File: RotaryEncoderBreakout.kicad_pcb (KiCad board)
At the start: 2 copper layers, 33 x 34.3 mm, 17 parts, among them J1 Conn_01x04_Male, J2 Conn_01x04_Male, J3 Conn_01x05_Male, SW1 RotaryEncoder_Switch_RGB, U1 WS2811

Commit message: Silkscreen refinement
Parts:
- SW1: value RotaryEncoder_Switch_RGB -> EC12PLRGB
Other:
- board text added: "J3: 1=PC3 2=Din 3=Dout Short 1-2 for Din=PC3 Short 4-5 for 400KHz / Open for 800KHz"
- board text removed: "J3: Din=2 Dout=3 Short 1-2 for Din=PC3 Short 4-5 for 400KHz / Open for 800KHz"
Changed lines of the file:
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@@
     (links 0)
     (no_connects 0)
-    (area 106.921 51.041 145.274 87.705001)
+    (area 109.779999 53.264999 142.950001 87.705001)
     (thickness 1.6)
     (drawings 17)
@@
       (effects (font (size 1 1) (thickness 0.15)))
     )
-    (fp_text value RotaryEncoder_Switch_RGB (at 12.065 1.27 90) (layer F.Fab)
-      (effects (font (size 1 1) (thickness 0.15)))
+    (fp_text value EC12PLRGB (at 6.858 -4.445 90) (layer F.SilkS)
+      (effects (font (size 0.635 0.635) (thickness 0.15)))
     )
     (fp_line (start -6.223 6.604) (end 6.223 6.604) (layer F.CrtYd) (width 0.15))
@@
     (descr "Through hole straight pin header, 1x05, 2.54mm pitch, single row")
     (tags "Through hole pin header THT 1x05 2.54mm single row")
-    (fp_text reference J3 (at 0 -3.175 360) (layer F.SilkS)
+    (fp_text reference J3 (at 0 -3.175 450) (layer F.SilkS)
       (effects (font (size 1 1) (thickness 0.15)))
     )
@@
       (effects (font (size 1 1) (thickness 0.15)))
     )
-    (fp_text value 10K (at 1.905 1.905) (layer F.SilkS)
+    (fp_text value 10K (at 1.27 1.905) (layer F.SilkS)
       (effects (font (size 0.635 0.635) (thickness 0.15)))
     )
@@
       (effects (font (size 1 1) (thickness 0.15)))
     )
-    (fp_text value 33 (at 1.905 1.905) (layer F.SilkS)
+    (fp_text value 33 (at 1.27 1.905) (layer F.SilkS)
       (effects (font (size 0.635 0.635) (thickness 0.15)))
     )
@@
       (effects (font (size 1 1) (thickness 0.15)))
     )
-    (fp_text value WS2811 (at 0 3.5 90) (layer F.Fab)
-      (effects (font (size 1 1) (thickness 0.15)))
+    (fp_text value WS2811 (at 0 -3.175 90) (layer F.SilkS)
+      (effects (font (size 0.635 0.635) (thickness 0.15)))
     )
     (fp_line (start -0.95 -2.45) (end 1.95 -2.45) (layer F.Fab) (width 0.15))
@@
     (effects (font (size 1.27 1.27) (thickness 0.3)) (justify mirror))
   )
-  (gr_text "J3: Din=2 Dout=3 Short 1-2 for Din=PC3\nShort 4-5 for 400KHz / Open for 800KHz" (at 140.97 70.485 90) (layer F.SilkS)
-    (effects (font (size 0.762 0.762) (thickness 0.1905)))
+  (gr_text "J3: 1=PC3 2=Din 3=Dout Short 1-2 for Din=PC3\nShort 4-5 for 400KHz / Open for 800KHz" (at 140.97 71.755 90) (layer F.SilkS)
+    (effects (font (size 0.635 0.635) (thickness 0.15875)))
   )
   (gr_arc (start 114.935 78.867) (end 114.935 77.597) (angle 90) (layer Edge.Cuts) (width 0.15))
   (gr_line (start 116.205 78.867) (end 116.205 87.63) (layer Edge.Cuts) (width 0.15))
   (gr_line (start 109.855 77.597) (end 114.935 77.597) (layer Edge.Cuts) (width 0.15))
-  (gr_text PC0 (at 115.57 68.326) (layer F.SilkS)
+  (gr_text PC0 (at 115.824 68.072) (layer F.SilkS)
     (effects (font (size 0.635 0.635) (thickness 0.127)))
   )
-  (gr_text PC1 (at 115.57 70.866) (layer F.SilkS)
+  (gr_text PC1 (at 115.824 70.612) (layer F.SilkS)
     (effects (font (size 0.635 0.635) (thickness 0.127)))
   )
-  (gr_text PC2 (at 115.57 73.406) (layer F.SilkS)
+  (gr_text PC2 (at 115.824 73.152) (layer F.SilkS)
     (effects (font (size 0.635 0.635) (thickness 0.127)))
   )
-  (gr_text 5V (at 115.57 55.245) (layer F.SilkS)
+  (gr_text 5V (at 115.824 55.245) (layer F.SilkS)
     (effects (font (size 0.635 0.635) (thickness 0.127)))
   )
-  (gr_text GND (at 115.57 57.785) (layer F.SilkS)
+  (gr_text GND (at 115.824 57.785) (layer F.SilkS)
     (effects (font (size 0.635 0.635) (thickness 0.127)))
   )
-  (gr_text GND (at 115.57 60.325) (layer F.SilkS)
+  (gr_text GND (at 115.824 60.325) (layer F.SilkS)
     (effects (font (size 0.635 0.635) (thickness 0.127)))
   )
-  (gr_text PC3 (at 115.57 75.946) (layer F.SilkS)
+  (gr_text PC3 (at 115.824 75.692) (layer F.SilkS)
     (effects (font (size 0.635 0.635) (thickness 0.127)))
   )
-  (gr_text Vin (at 115.57 62.865) (layer F.SilkS)
+  (gr_text Vin (at 115.824 62.865) (layer F.SilkS)
     (effects (font (size 0.635 0.635) (thickness 0.127)))
   )

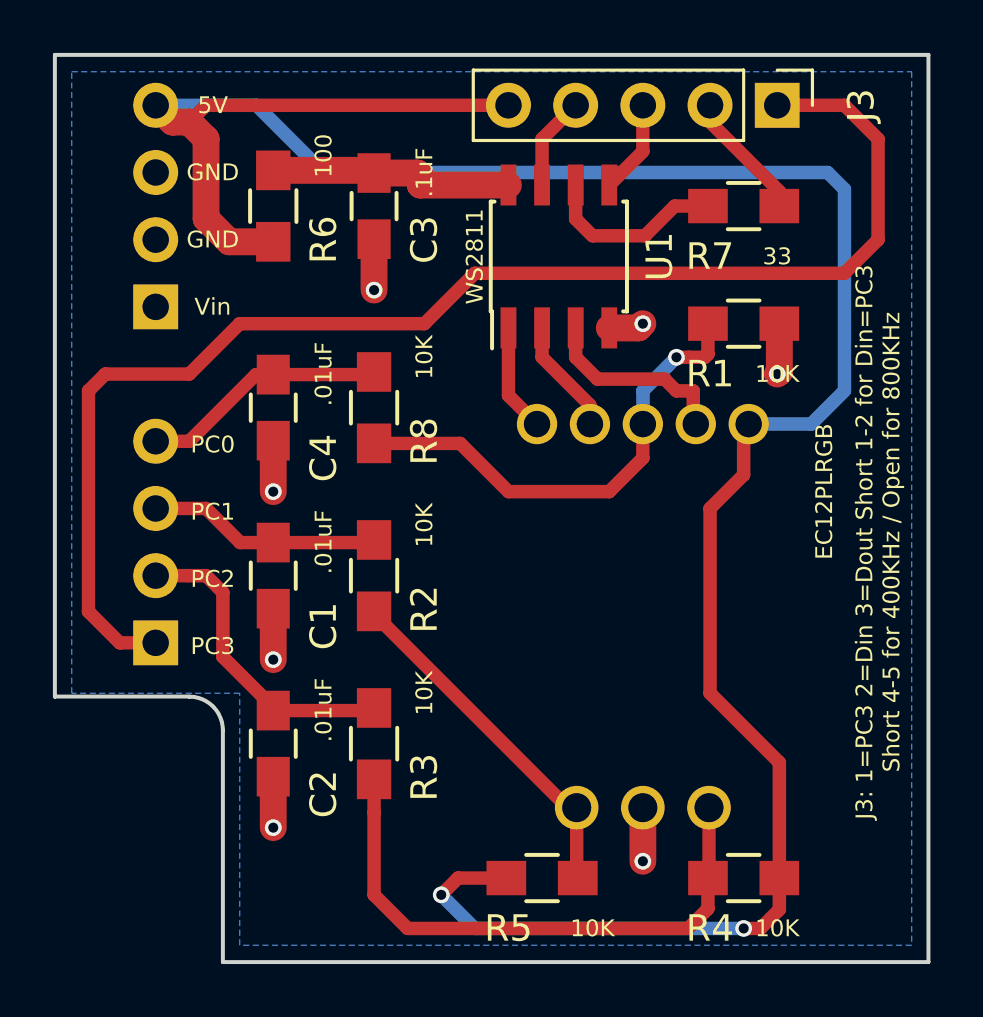
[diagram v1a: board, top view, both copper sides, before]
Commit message: Update component values
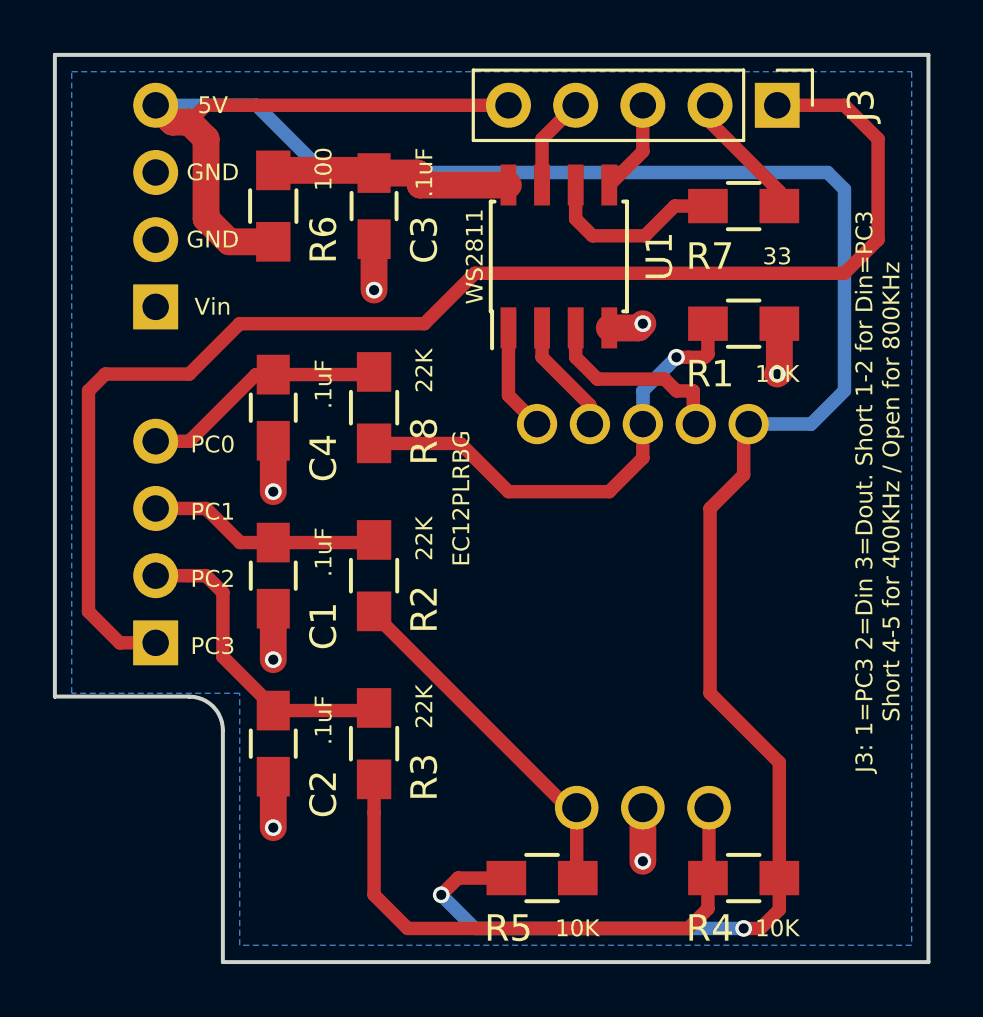
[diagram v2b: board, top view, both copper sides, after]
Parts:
- C1, C2, C4: value .01uF -> .1uF
- R2, R3, R8: value 10K -> 22K
- SW1: value EC12PLRGB -> EC12PLRBG
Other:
- board text added: "J3: 1=PC3 2=Din 3=Dout. Short 1-2 for Din=PC3 Short 4-5 for 400KHz / Open for 800KHz"
- board text removed: "J3: 1=PC3 2=Din 3=Dout Short 1-2 for Din=PC3 Short 4-5 for 400KHz / Open for 800KHz"
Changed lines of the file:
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@@
 (kicad_pcb (version 4) (host pcbnew 4.0.7)
   (general
-    (links 0)
+    (links 35)
     (no_connects 0)
     (area 109.779999 53.264999 142.950001 87.705001)
@@
     (0 F.Cu signal)
     (31 B.Cu signal)
-    (32 B.Adhes user)
-    (33 F.Adhes user)
+    (32 B.Adhes user hide)
+    (33 F.Adhes user hide)
     (34 B.Paste user)
     (35 F.Paste user)
@@
       (effects (font (size 1 1) (thickness 0.15)))
     )
-    (fp_text value EC12PLRGB (at 6.858 -4.445 90) (layer F.SilkS)
+    (fp_text value EC12PLRBG (at -6.858 -4.191 90) (layer F.SilkS)
       (effects (font (size 0.635 0.635) (thickness 0.15)))
     )
@@
       (effects (font (size 1 1) (thickness 0.15)))
     )
-    (fp_text value .01uF (at -1.27 -1.905 270) (layer F.SilkS)
+    (fp_text value .1uF (at -0.889 -1.905 270) (layer F.SilkS)
       (effects (font (size 0.635 0.635) (thickness 0.15)))
     )
@@
       (effects (font (size 1 1) (thickness 0.15)))
     )
-    (fp_text value .01uF (at -1.27 -1.905 270) (layer F.SilkS)
+    (fp_text value .1uF (at -0.889 -1.905 270) (layer F.SilkS)
       (effects (font (size 0.635 0.635) (thickness 0.15)))
     )
@@
       (effects (font (size 1 1) (thickness 0.15)))
     )
-    (fp_text value .01uF (at -1.27 -1.905 270) (layer F.SilkS)
+    (fp_text value .1uF (at -0.889 -1.905 270) (layer F.SilkS)
       (effects (font (size 0.635 0.635) (thickness 0.15)))
     )
@@
       (effects (font (size 1 1) (thickness 0.15)))
     )
-    (fp_text value 10K (at 1.905 1.905 90) (layer F.SilkS)
+    (fp_text value 22K (at 1.397 1.905 90) (layer F.SilkS)
       (effects (font (size 0.635 0.635) (thickness 0.15)))
     )
@@
       (effects (font (size 1 1) (thickness 0.15)))
     )
-    (fp_text value 10K (at 1.905 1.905 90) (layer F.SilkS)
+    (fp_text value 22K (at 1.397 1.905 90) (layer F.SilkS)
       (effects (font (size 0.635 0.635) (thickness 0.15)))
     )
@@
       (effects (font (size 1 1) (thickness 0.15)))
     )
-    (fp_text value 10K (at 1.905 1.905) (layer F.SilkS)
+    (fp_text value 10K (at 1.33 1.905) (layer F.SilkS)
       (effects (font (size 0.635 0.635) (thickness 0.15)))
     )
@@
       (effects (font (size 1 1) (thickness 0.15)))
     )
-    (fp_text value 100 (at 1.905 1.905 90) (layer F.SilkS)
+    (fp_text value 100 (at 1.397 1.905 90) (layer F.SilkS)
       (effects (font (size 0.635 0.635) (thickness 0.15)))
     )
@@
       (effects (font (size 1 1) (thickness 0.15)))
     )
-    (fp_text value 10K (at 1.905 1.905 90) (layer F.SilkS)
+    (fp_text value 22K (at 1.397 1.905 90) (layer F.SilkS)
       (effects (font (size 0.635 0.635) (thickness 0.15)))
     )
@@
     (effects (font (size 1.27 1.27) (thickness 0.3)) (justify mirror))
   )
-  (gr_text "J3: 1=PC3 2=Din 3=Dout Short 1-2 for Din=PC3\nShort 4-5 for 400KHz / Open for 800KHz" (at 140.97 71.755 90) (layer F.SilkS)
+  (gr_text "J3: 1=PC3 2=Din 3=Dout. Short 1-2 for Din=PC3\nShort 4-5 for 400KHz / Open for 800KHz" (at 140.97 69.85 90) (layer F.SilkS)
     (effects (font (size 0.635 0.635) (thickness 0.15875)))
   )
